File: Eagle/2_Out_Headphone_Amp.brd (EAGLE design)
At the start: 100 x 80 mm, 29 parts, among them IC1 OPA2134P, IC2 OPA2134P, IC3 OPA2134P

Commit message: 基板設計図修正
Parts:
- moved C11 2.54 mm to (50.8, 43.2)
- moved C2 2.54 mm to (63.5, 43.2)
- moved R4 2.54 mm to (50.8, 36.8)
- moved R7 2.54 mm to (50.8, 16.5)
- moved R10 2.54 mm to (24.1, 25.4)
- moved R2 2.54 mm to (24.1, 27.9)
- moved C1 2.54 mm to (61.0, 33.0)
- moved C10 2.54 mm to (35.6, 33.0)
- moved C4 2.54 mm to (55.9, 25.4)
- moved C5 2.54 mm to (43.2, 27.9)
- moved C6 2.54 mm to (22.9, 20.3)
- moved C7 2.54 mm to (35.6, 17.8)
- moved C8 2.54 mm to (22.9, 35.6)
- moved C9 2.54 mm to (61.0, 20.3)
- moved IC1 2.54 mm to (49.5, 26.7)
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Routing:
- net GND: track 194.1 -> 192.6 mm

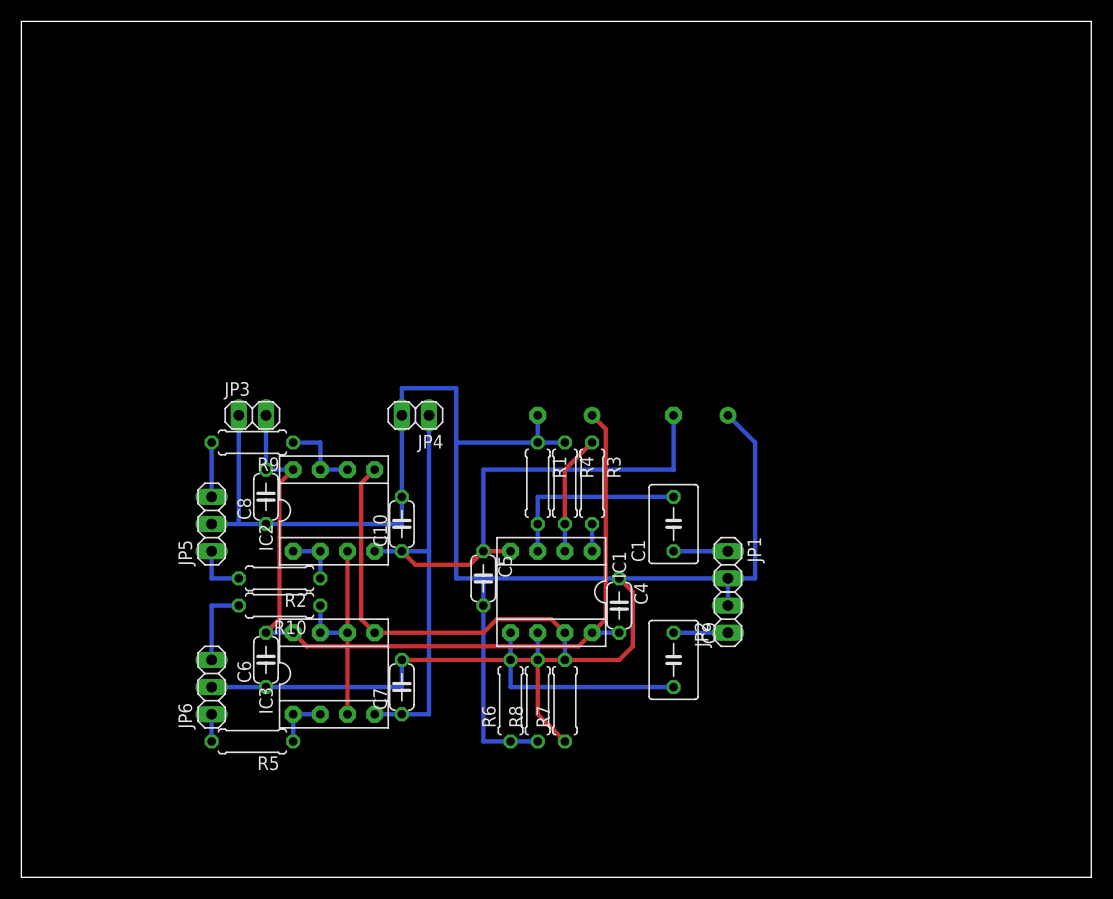
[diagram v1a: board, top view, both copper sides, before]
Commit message: 基板配線図修正 Cサイズフルに
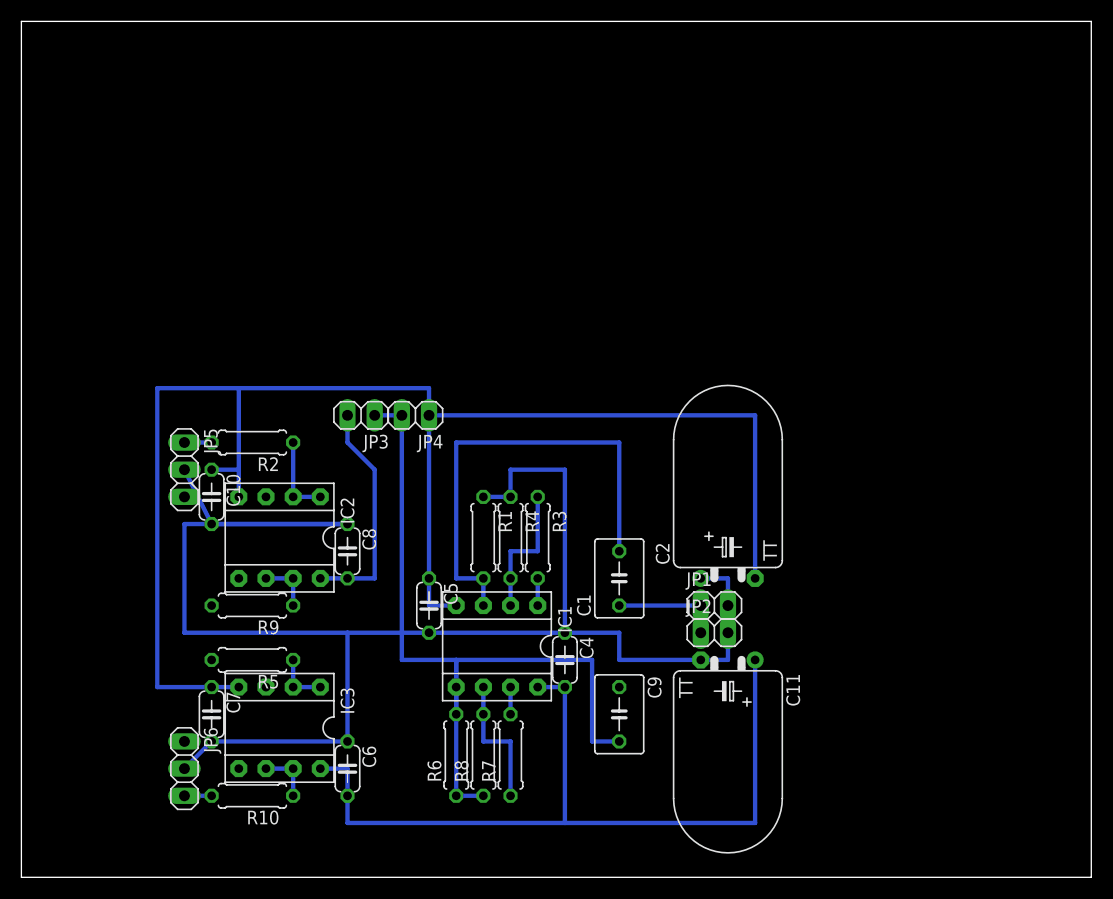
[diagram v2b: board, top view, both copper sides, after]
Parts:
- moved C11 27.5 mm to (66.0, 20.3), flipped to the top, turned to 180 degrees
- moved C10 18.0 mm to (17.8, 35.6), turned to 270 degrees
- moved C7 18.0 mm to (17.8, 15.2), turned to 270 degrees
- moved R10 18.0 mm to (21.6, 7.62)
- moved C2 15.5 mm to (66.0, 27.9), flipped to the top
- moved R9 15.2 mm to (21.6, 25.4)
- moved R2 13.0 mm to (21.6, 40.6)
- moved C6 12.7 mm to (30.5, 10.2), turned to 270 degrees
- moved JP3 10.2 mm to (31.8, 43.2), turned to 180 degrees
- moved C8 9.16 mm to (30.5, 30.5), turned to 270 degrees
- moved JP6 8.03 mm to (15.2, 10.2), turned to 270 degrees
- moved R5 7.62 mm to (21.6, 20.3)
- moved C4 7.18 mm to (50.8, 20.3)
- moved R3 7.18 mm to (48.3, 31.8)
- moved IC3 7.18 mm to (24.1, 14.0), turned to 180 degrees
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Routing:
- net V-: track 79.8 -> 142.2 mm
- net N$12: track 37.7 -> 2.54 mm
- net N$2: track 17.8 -> 43.2 mm
- net V+: track 79.4 -> 97.6 mm
- net N$4: track 17.8 -> 2.54 mm
- net GND: track 192.6 -> 204.9 mm
- net N$10: track 20.3 -> 27.9 mm
- net N$9: track 5.08 -> 0.00 mm
- net N$15: track 5.08 -> 0.00 mm
- net N$16: track 7.62 -> 2.54 mm
- net N$8: track 2.54 -> 0.00 mm
- net N$5: track 5.08 -> 7.62 mm
- net N$13: track 7.62 -> 5.08 mm
- net N$6: track 5.08 -> 2.54 mm
- net N$1: track 5.08 -> 7.62 mm
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
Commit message: 基板設計図微調整前
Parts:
- moved C9 10.8 mm to (48.3, 22.9)
- moved JP3 10.5 mm to (21.6, 40.6)
- moved JP5 9.16 mm to (7.62, 33.0)
- moved JP6 9.16 mm to (7.62, 15.2)
- moved C1 8.03 mm to (48.3, 30.5)
- moved C11 8.03 mm to (58.4, 22.9)
- moved C2 8.03 mm to (58.4, 30.5), flipped to the bottom
- moved C7 8.03 mm to (10.2, 17.8)
- moved C6 8.03 mm to (22.9, 12.7)
- moved R5 8.03 mm to (14.0, 22.9)
- moved JP1 8.03 mm to (57.1, 27.9)
- moved JP2 8.03 mm to (57.1, 25.4)
- moved JP4 8.03 mm to (29.2, 40.6)
- moved IC1 7.62 mm to (36.8, 21.6)
- moved C10 7.62 mm to (10.2, 35.6)
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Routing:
- net V+: track 97.6 -> 219.5 mm
- net GND: track 204.9 -> 154.9 mm
- net V-: track 142.2 -> 112.8 mm
- net N$10: track 27.9 -> 2.54 mm
- net N$12: track 2.54 -> 15.2 mm
- net N$9: track 0.00 -> 7.62 mm
- net N$15: track 0.00 -> 7.62 mm
- net N$16: track 2.54 -> 7.62 mm
- net N$2: track 43.2 -> 40.6 mm
- net N$6: track 2.54 -> 0.00 mm
- net N$7: track 5.08 -> 7.62 mm
- net N$3: track 12.7 -> 10.6 mm
- net N$11: track 12.7 -> 10.6 mm

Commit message: 基板設計図 抵抗を立てる前
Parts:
- moved R10 2.54 mm to (16.5, 7.62)
- moved R2 2.54 mm to (16.5, 40.6)
- moved R5 2.54 mm to (16.5, 22.9)
- moved R9 2.54 mm to (16.5, 25.4)
- moved JP5 2.54 mm to (10.2, 33.0)
- moved JP6 2.54 mm to (10.2, 15.2)
- moved C10 2.54 mm to (12.7, 35.6)
- moved C11 2.54 mm to (55.9, 22.9)
- moved C2 2.54 mm to (55.9, 30.5)
- moved C6 2.54 mm to (25.4, 12.7)
- moved C7 2.54 mm to (12.7, 17.8)
- moved C8 2.54 mm to (25.4, 30.5)
- moved IC2 2.54 mm to (19.1, 31.8)
- moved IC3 2.54 mm to (19.1, 14.0)
- moved JP1 2.54 mm to (54.6, 27.9)
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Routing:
- net N$4: track 2.54 -> 20.3 mm
- net N$12: track 15.2 -> 33.0 mm
- net V+: track 219.5 -> 203.2 mm
- net GND: track 154.9 -> 139.7 mm
- net V-: track 112.8 -> 102.7 mm
- net N$3: track 10.6 -> 2.54 mm
- net N$8: track 0.00 -> 5.68 mm
- net N$6: track 0.00 -> 5.68 mm
- net N$2: track 40.6 -> 35.6 mm
- net N$9: track 7.62 -> 5.08 mm
- net N$1: track 7.62 -> 5.08 mm

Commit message: 基板設計図の変更
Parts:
- R1, R4, R6, R7, R8: device rcl:0207/7 -> rcl:0207/2V
- moved JP1 8.03 mm to (62.2, 25.4)
- moved R6 3.59 mm to (30.5, 14.0)
- moved R8 3.59 mm to (33.0, 14.0)
- moved C11 3.59 mm to (58.4, 20.3)
- moved C1 2.54 mm to (50.8, 30.5)
- moved C2 2.54 mm to (58.4, 30.5)
- moved C9 2.54 mm to (50.8, 22.9)
- moved JP2 2.54 mm to (57.1, 25.4)
- moved R1 2.54 mm to (35.6, 29.2)
- moved R4 2.54 mm to (38.1, 29.2)
- moved R7 1.80 mm to (36.8, 12.7), turned to 0 degrees
- moved R3 1.80 mm to (41.9, 33.0), turned to 0 degrees
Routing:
- net GND: track 139.7 -> 196.6 mm
- net N$4: track 20.3 -> 57.5 mm
- net V+: track 203.2 -> 231.3 mm
- net N$10: track 2.54 -> 25.4 mm
- net N$12: track 33.0 -> 49.9 mm
- net N$3: track 2.54 -> 12.7 mm
- net N$1: track 5.08 -> 12.7 mm
- net V-: track 102.7 -> 106.7 mm
- net N$11: track 10.6 -> 7.62 mm
- net N$2: track 35.6 -> 36.6 mm
